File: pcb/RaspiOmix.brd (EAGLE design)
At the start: 85 x 56 mm, 49 parts, among them IC1 MCP3424-E/SL, IC2 DS1307

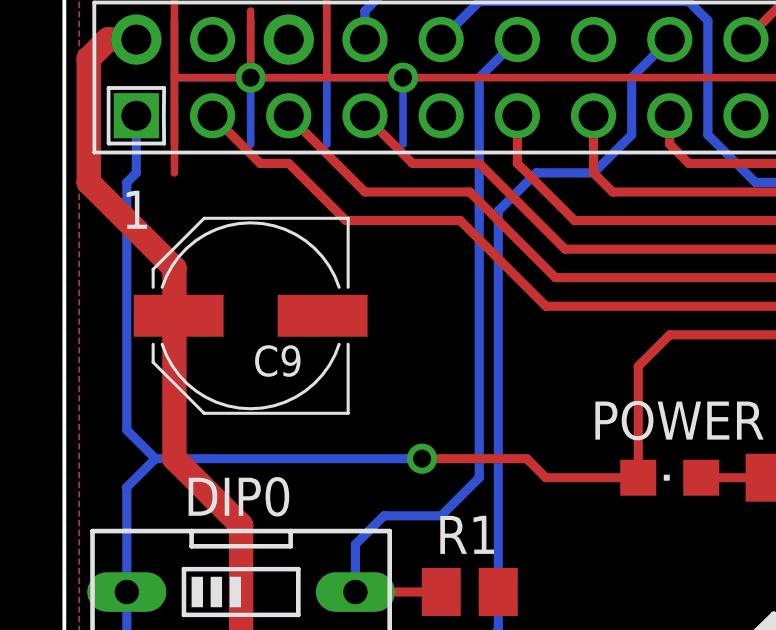
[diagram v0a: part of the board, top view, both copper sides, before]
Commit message: Move C9 label
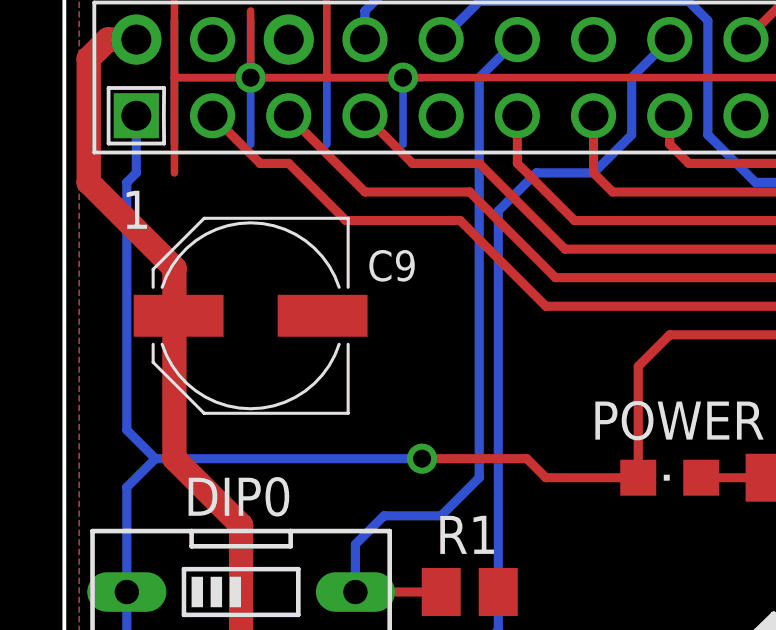
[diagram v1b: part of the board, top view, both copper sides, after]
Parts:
- R14: value 470 -> 330
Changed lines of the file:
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@@
 <attribute name="VALUE" x="21.59" y="41.275" size="1.27" layer="27" rot="R180"/>
 </element>
-<element name="R14" library="rcl" package="M0805" value="470" x="24.4475" y="38.735" smashed="yes" rot="R180">
+<element name="R14" library="rcl" package="M0805" value="330" x="24.4475" y="38.735" smashed="yes" rot="R180">
 <attribute name="NAME" x="29.845" y="39.37" size="1.27" layer="25" rot="R180"/>
 <attribute name="VALUE" x="25.7175" y="41.275" size="1.27" layer="27" rot="R180"/>
@@
 <attribute name="VALUE" x="16.7575" y="18.895" size="1.016" layer="27" rot="R270"/>
 </element>
-<element name="C9" library="rcl" package="PANASONIC_D" value="220uf" x="6.35" y="44.1325" rot="R180"/>
+<element name="C9" library="rcl" package="PANASONIC_D" value="220uf" x="6.35" y="44.1325" smashed="yes" rot="R180">
+<attribute name="NAME" x="11.91" y="46.3075" size="1.016" layer="25" rot="R180"/>
+<attribute name="VALUE" x="8.1" y="46.1075" size="1.016" layer="27" rot="R180"/>
+</element>
 <element name="U$1" library="ohw-logo" package="OSHW_FILLX350_NOTEXT" value="" x="21.9075" y="26.3525"/>
 <element name="TP1" library="testpad" package="P1-13" value="TPPAD1-13" x="2.54" y="27.305" smashed="yes">

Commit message: Petite modif
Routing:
- net +5V: track 281.2 -> 280.6 mm
- net PI_DIP0: track 24.6 -> 25.2 mm
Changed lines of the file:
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@@
 </element>
 <element name="C9" library="rcl" package="PANASONIC_D" value="220uf" x="6.35" y="44.1325" smashed="yes" rot="R180">
-<attribute name="NAME" x="11.91" y="46.3075" size="1.016" layer="25" rot="R180"/>
+<attribute name="NAME" x="11.91" y="46.9425" size="1.016" layer="25" rot="R180"/>
 <attribute name="VALUE" x="8.1" y="46.1075" size="1.016" layer="27" rot="R180"/>
 </element>
@@
 <wire x1="54.2925" y1="46.355" x2="52.07" y2="46.355" width="0.3048" layer="1"/>
 <wire x1="52.07" y1="46.355" x2="51.435" y2="46.99" width="0.3048" layer="1"/>
-<wire x1="51.435" y1="46.99" x2="51.435" y2="49.53" width="0.3048" layer="1"/>
-<wire x1="51.435" y1="49.53" x2="52.07" y2="50.165" width="0.3048" layer="1"/>
-<wire x1="52.07" y1="50.165" x2="56.1975" y2="50.165" width="0.3048" layer="1"/>
-<wire x1="56.88" y1="48.26" x2="56.88" y2="49.4825" width="0.3048" layer="1"/>
-<wire x1="56.88" y1="49.4825" x2="56.1975" y2="50.165" width="0.3048" layer="1"/>
+<wire x1="51.435" y1="46.99" x2="51.435" y2="49.2125" width="0.3048" layer="1"/>
+<wire x1="51.435" y1="49.2125" x2="52.07" y2="49.8475" width="0.3048" layer="1"/>
+<wire x1="52.07" y1="49.8475" x2="56.1975" y2="49.8475" width="0.3048" layer="1"/>
+<wire x1="56.88" y1="48.26" x2="56.88" y2="49.165" width="0.3048" layer="1"/>
+<wire x1="56.88" y1="49.165" x2="56.1975" y2="49.8475" width="0.3048" layer="1"/>
 <wire x1="3.81" y1="45.72" x2="3.81" y2="44.2725" width="0" layer="19" extent="1-1"/>
 </signal>
@@
 <contactref element="C28" pad="2"/>
 <wire x1="2.2225" y1="34.925" x2="2.2225" y2="32.385" width="0.3048" layer="16"/>
-<wire x1="12.065" y1="39.37" x2="15.5575" y2="39.37" width="0.3048" layer="1"/>
-<wire x1="15.5575" y1="39.37" x2="16.1925" y2="38.735" width="0.3048" layer="1"/>
-<wire x1="16.1925" y1="38.735" x2="19.27" y2="38.735" width="0.3048" layer="1"/>
-<via x="12.065" y="39.37" extent="1-16" drill="0.6"/>
+<wire x1="12.065" y1="38.735" x2="19.27" y2="38.735" width="0.3048" layer="1"/>
+<via x="12.065" y="38.735" extent="1-16" drill="0.6"/>
 <wire x1="56.455" y1="12.3825" x2="58.1025" y2="12.3825" width="0.3048" layer="1"/>
 <wire x1="58.1025" y1="12.3825" x2="58.42" y2="12.7" width="0.3048" layer="1"/>
@@
 <wire x1="62.865" y1="33.02" x2="62.865" y2="24.765" width="0.3048" layer="1"/>
 <wire x1="62.865" y1="24.765" x2="62.865" y2="22.5425" width="0.3048" layer="1"/>
-<wire x1="2.2225" y1="34.925" x2="2.2225" y2="38.4175" width="0.3048" layer="16"/>
-<wire x1="2.2225" y1="38.4175" x2="3.175" y2="39.37" width="0.3048" layer="16"/>
-<wire x1="12.065" y1="39.37" x2="3.175" y2="39.37" width="0.3048" layer="16"/>
-<wire x1="3.175" y1="39.37" x2="2.2225" y2="40.3225" width="0.3048" layer="16"/>
-<wire x1="2.2225" y1="40.3225" x2="2.2225" y2="48.5775" width="0.3048" layer="16"/>
+<wire x1="2.2225" y1="34.925" x2="2.2225" y2="37.7825" width="0.3048" layer="16"/>
+<wire x1="2.2225" y1="37.7825" x2="3.175" y2="38.735" width="0.3048" layer="16"/>
+<wire x1="12.065" y1="38.735" x2="3.175" y2="38.735" width="0.3048" layer="16"/>
+<wire x1="3.175" y1="38.735" x2="2.2225" y2="39.6875" width="0.3048" layer="16"/>
+<wire x1="2.2225" y1="39.6875" x2="2.2225" y2="48.5775" width="0.3048" layer="16"/>
 <wire x1="2.2225" y1="48.5775" x2="2.54" y2="48.895" width="0.3048" layer="16"/>
 <wire x1="2.54" y1="48.895" x2="2.54" y2="50.8" width="0.3048" layer="16"/>
@@
 <contactref element="U$3" pad="12"/>
 <wire x1="15.24" y1="53.34" x2="13.97" y2="52.07" width="0.3048" layer="16"/>
-<wire x1="13.97" y1="52.07" x2="13.97" y2="38.735" width="0.3048" layer="16"/>
-<wire x1="13.97" y1="38.735" x2="12.7" y2="37.465" width="0.3048" layer="16"/>
+<wire x1="13.97" y1="52.07" x2="13.97" y2="36.195" width="0.3048" layer="16"/>
+<wire x1="13.97" y1="36.195" x2="12.7" y2="34.925" width="0.3048" layer="16"/>
 <contactref element="SW1" pad="4"/>
 <contactref element="R1" pad="2"/>
-<wire x1="9.8425" y1="34.925" x2="9.8425" y2="36.5125" width="0.3048" layer="16"/>
-<wire x1="9.8425" y1="36.5125" x2="10.795" y2="37.465" width="0.3048" layer="16"/>
-<wire x1="10.795" y1="37.465" x2="12.7" y2="37.465" width="0.3048" layer="16"/>
+<wire x1="9.8425" y1="34.925" x2="12.7" y2="34.925" width="0.3048" layer="16"/>
 <wire x1="12.7025" y1="34.925" x2="9.8425" y2="34.925" width="0.3048" layer="1"/>
 </signal>

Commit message: PCB
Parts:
- added JP1: (no value), jumper:JP1
- added SJ1: (no value), jumper:SJ
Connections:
- net IO0: now also CON_IO_3.2
- net IO1: now also CON_IO_0.2
- net IO2: now also CON_IO_1.2
- net IO3: now also CON_IO_2.2
- net N$1: now also CON_AN_3.2
- net N$2: now also CON_AN_0.2
- net N$3: now also CON_AN_1.2
- net N$58: now also JP1.1, SJ1.2
- net N$8: now also CON_AN_2.2
- net PI_DIP0: now also U$3.7; no longer U$3.12
- net PI_IO0: now also U$3.12; no longer U$3.7
- net VSS: now also JP1.2, SJ1.1
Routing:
- net IO0: track 16.8 -> 56.4 mm
- net N$1: track 11.5 -> 48.8 mm, vias 0 -> 1
- net N$3: track 5.83 -> 21.3 mm
- net N$8: track 18.6 -> 31.4 mm, vias 0 -> 1
- net IO1: track 7.80 -> 19.0 mm
- net N$2: track 9.57 -> 18.6 mm, vias 0 -> 1
- net N$58: track 16.1 -> 22.7 mm
- net VSS: track 91.3 -> 84.9 mm, vias 6 -> 7
- net IO2: track 10.3 -> 13.7 mm
- net IO3: track 21.3 -> 22.5 mm
- net PI_DIP1: track 31.3 -> 31.9 mm
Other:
- board text added: "rev 1.1.0 ---"
- board text removed: "rev 1.0.8"

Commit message: PCB 1.1.1
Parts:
- added IO6: TPPAD1-13, testpad:P1-13
- R20, R22, R24, R26: value 10k -> 10k 1%
- R21, R23, R25, R27: value 6.8k -> 6.8k 1%
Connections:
- net N$1 renamed AN0
- net N$2 renamed AN1
- net N$3 renamed AN2
- net N$8 renamed AN3
- new net PI_IO6: IO6.TP, U$3.22
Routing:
- net VSS: track 84.9 -> 63.6 mm
- net PI_IO6: track 0.00 -> 8.43 mm
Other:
- board text added: "0"
- board text added: "1"
- board text added: "2"
- board text added: "3"
- board text added: "rev 1.1.0"
- board text added: "www.digitalspirit.org hugo, 10/2013"
- board text removed: "rev 1.1.0 ---"
- board text removed: "www.digitalspirit.org hugo, 06/2013"

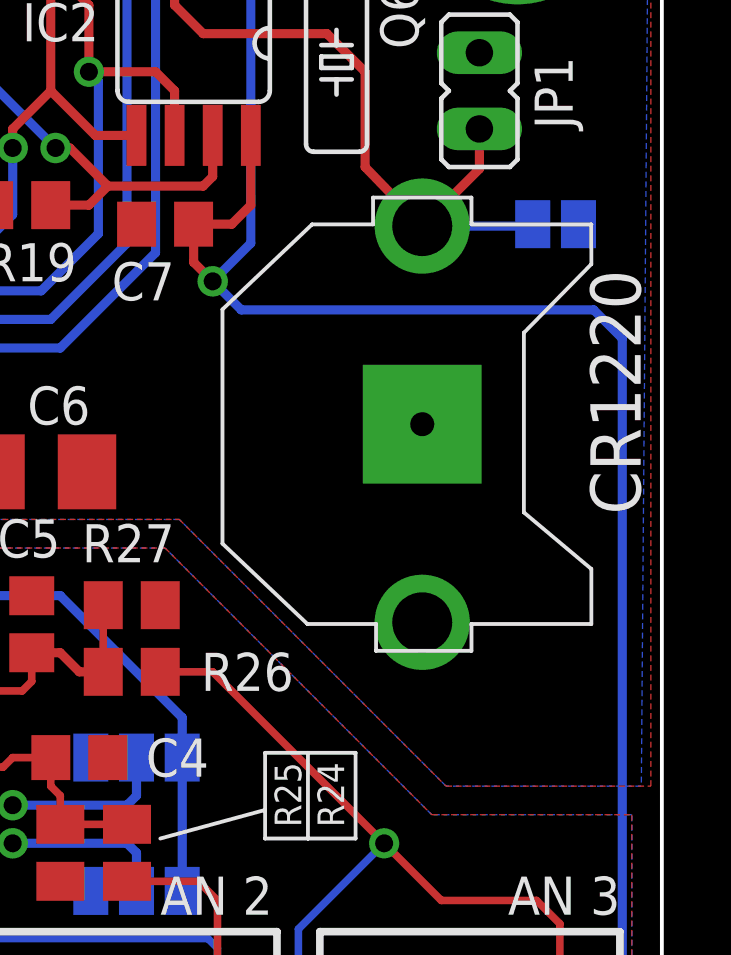
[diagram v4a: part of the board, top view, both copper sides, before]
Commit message: New RaspiO'Mix+ hat
Schema + PCB in progress…
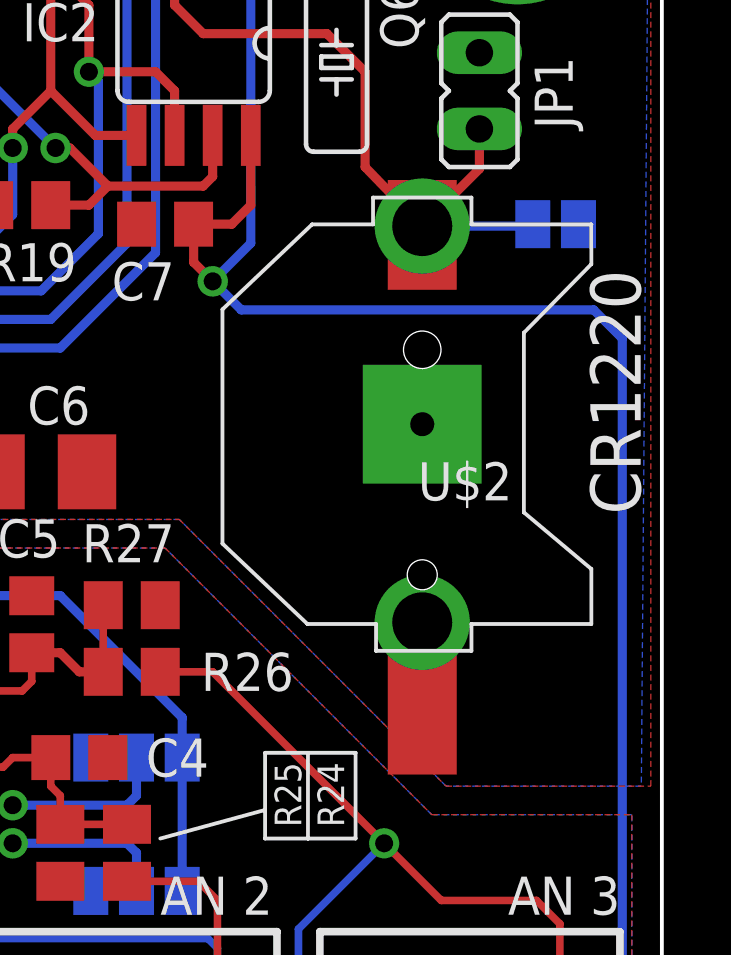
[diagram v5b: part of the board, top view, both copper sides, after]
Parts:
- added U$2: CR1220-HOLDER, battery-holder:HARWIN-CR1220
- R20, R22, R24, R26: value 10k 1% -> 10k 0.1%
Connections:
- net N$58: now also U$2.POS
- net VSS: now also U$2.NEG
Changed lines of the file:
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@@
 <attribute name="VALUE" x="14.9225" y="34.925" size="1.27" layer="27" rot="R180"/>
 </element>
-<element name="R26" library="rcl" package="M0805" value="10k 1%" x="67.46875" y="18.0975" smashed="yes">
+<element name="R26" library="rcl" package="M0805" value="10k 0.1%" x="67.46875" y="18.0975" smashed="yes">
 <attribute name="NAME" x="72.86625" y="18.7325" size="1.27" layer="25" rot="R180"/>
 <attribute name="VALUE" x="66.19875" y="15.5575" size="1.27" layer="27"/>
 </element>
-<element name="R24" library="rcl" package="M0805" value="10k 1%" x="67.31" y="12.065" smashed="yes" rot="R270">
+<element name="R24" library="rcl" package="M0805" value="10k 0.1%" x="67.31" y="12.065" smashed="yes" rot="R270">
 <attribute name="NAME" x="73.66" y="15.08125" size="0.889" layer="25" rot="R270"/>
 <attribute name="VALUE" x="64.77" y="13.335" size="1.27" layer="27" rot="R270"/>
 </element>
-<element name="R22" library="rcl" package="M0805" value="10k 1%" x="53.0225" y="13.335" smashed="yes" rot="R270">
+<element name="R22" library="rcl" package="M0805" value="10k 0.1%" x="53.0225" y="13.335" smashed="yes" rot="R270">
 <attribute name="NAME" x="49.68875" y="12.065" size="0.889" layer="25"/>
 <attribute name="VALUE" x="50.4825" y="14.605" size="1.27" layer="27" rot="R270"/>
 </element>
-<element name="R20" library="rcl" package="M0805" value="10k 1%" x="48.26" y="19.3675" smashed="yes" rot="R180">
+<element name="R20" library="rcl" package="M0805" value="10k 0.1%" x="48.26" y="19.3675" smashed="yes" rot="R180">
 <attribute name="NAME" x="46.6725" y="20.6375" size="1.27" layer="25"/>
 <attribute name="VALUE" x="49.53" y="21.9075" size="1.27" layer="27" rot="R180"/>
@@
 <attribute name="VALUE" x="33.3375" y="48.26" size="0.0254" layer="27"/>
 </element>
+<element name="U$2" library="battery-holder" package="HARWIN-CR1220" value="CR1220-HOLDER" x="77.1525" y="25.0825" rot="R180"/>
 </elements>
 <signals>
@@
 <contactref element="SJ1" pad="1"/>
 <contactref element="JP1" pad="2"/>
+<contactref element="U$2" pad="NEG"/>
 <wire x1="8.89" y1="54.61" x2="9.8425" y2="54.9275" width="0" layer="19" extent="1-1"/>
 <wire x1="66.1035" y1="15.24" x2="66.6725" y2="15.24" width="0" layer="19" extent="1-16"/>
@@
 <wire x1="79.0575" y1="36.195" x2="79.0575" y2="34.8615" width="0.3048" layer="1"/>
 <wire x1="79.0575" y1="34.8615" x2="77.1525" y2="32.9565" width="0.3048" layer="1"/>
+<contactref element="U$2" pad="POS"/>
+<wire x1="77.1525" y1="32.6625" x2="77.1525" y2="32.9565" width="0" layer="19" extent="1-16"/>
 </signal>
 <signal name="INTC">

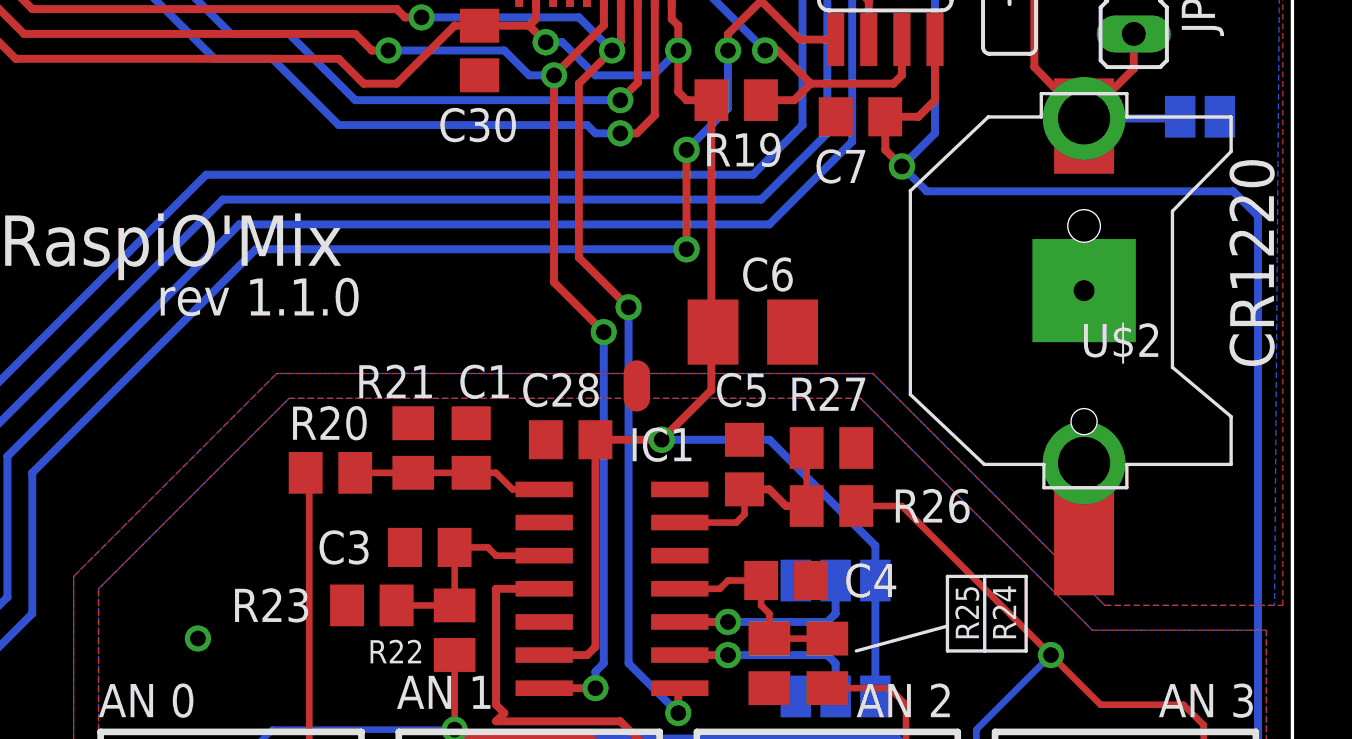
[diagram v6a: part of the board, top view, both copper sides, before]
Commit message: RaspiO'Mix+ -> Pcb 2.0.0
New RaspiO’Mix+ pcbs version is 2.0.0.
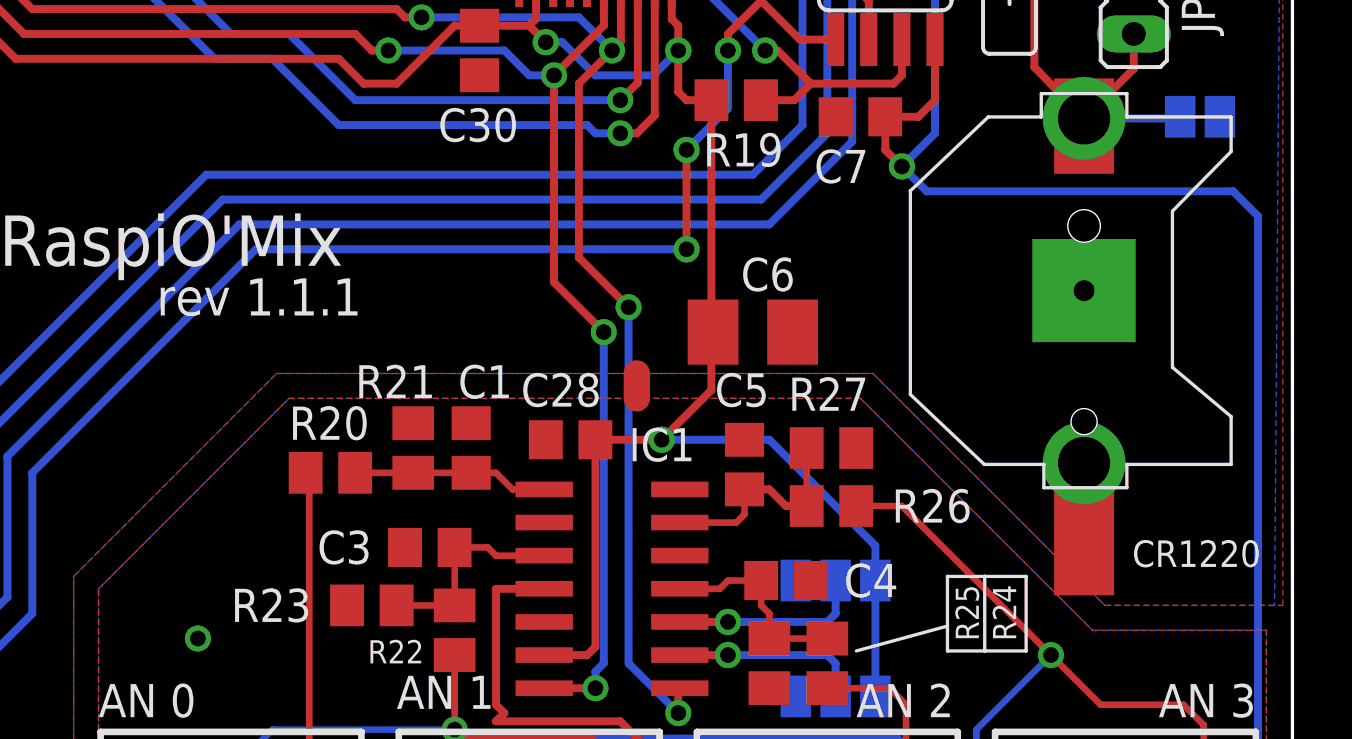
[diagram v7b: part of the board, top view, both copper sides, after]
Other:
- board text added: "rev 1.1.1"
- board text removed: "rev 1.1.0"
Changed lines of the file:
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@@
 <?xml version="1.0" encoding="utf-8"?>
 <!DOCTYPE eagle SYSTEM "eagle.dtd">
-<eagle version="7.1.0">
+<eagle version="7.2.0">
 <drawing>
 <settings>
@@
 <text x="4.1275" y="37.465" size="1.27" layer="25">DIP0</text>
 <text x="4.1275" y="28.575" size="1.27" layer="25">DIP1</text>
-<text x="41.5925" y="25.4" size="1.4224" layer="25">rev 1.1.0</text>
+<text x="41.5925" y="25.4" size="1.4224" layer="25">rev 1.1.1</text>
 <text x="35.56" y="27.305" size="1.9304" layer="25">RaspiO'Mix</text>
 <text x="22.225" y="24.13" size="1.4224" layer="25">CC-BY-SA </text>
@@
 <element name="C31" library="rcl" package="C0805" value="100nf" x="53.6575" y="45.085" rot="R180"/>
 <element name="CR1220" library="adafruit" package="CR1220-THM" value="" x="77.1525" y="26.3525" smashed="yes" rot="R270">
-<attribute name="NAME" x="82.7545" y="31.496" size="1.6764" layer="25" font="vector" rot="R270"/>
+<attribute name="NAME" x="78.994" y="15.762" size="1.016" layer="25" font="vector"/>
 <attribute name="VALUE" x="72.6025" y="30.6705" size="1.6764" layer="27" font="vector" rot="R270"/>
 </element>
@@
 <attribute name="VALUE" x="33.3375" y="48.26" size="0.0254" layer="27"/>
 </element>
-<element name="U$2" library="battery-holder" package="HARWIN-CR1220" value="CR1220-HOLDER" x="77.1525" y="25.0825" rot="R180"/>
+<element name="U$2" library="battery-holder" package="HARWIN-CR1220" value="CR1220-HOLDER" x="77.1525" y="25.0825" smashed="yes" rot="R180">
+<attribute name="NAME" x="80.1525" y="25.0825" size="1.27" layer="25" rot="R180" display="off"/>
+<attribute name="VALUE" x="80.1525" y="26.8325" size="1.27" layer="27" rot="R180"/>
+</element>
 </elements>
 <signals>
